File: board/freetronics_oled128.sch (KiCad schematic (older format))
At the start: 38 parts, among them IC1 TPS61040, P1 M02X05, P2 MICROSD, P3 M02X02, P4 M02X02, Q1 2N7002, SW1 SW_PUSHBUTTON, SW2 SW_PUSHBUTTON, U1 MC74VHCT50A

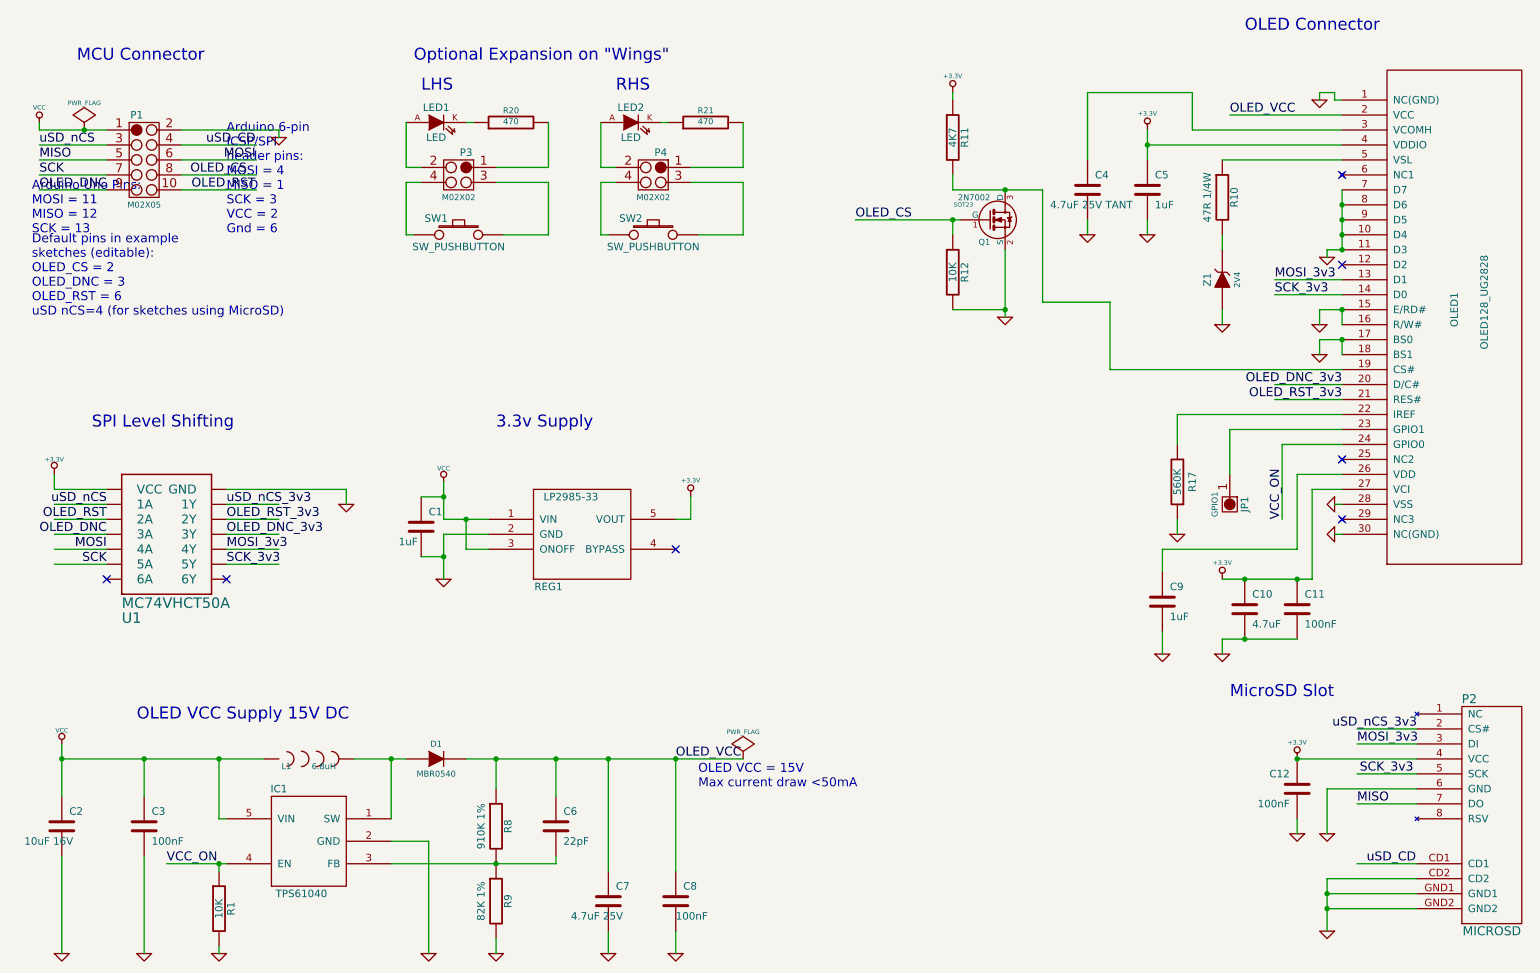
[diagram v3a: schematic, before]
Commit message: Backannotate footprints into schematic, minor labelling cleanups
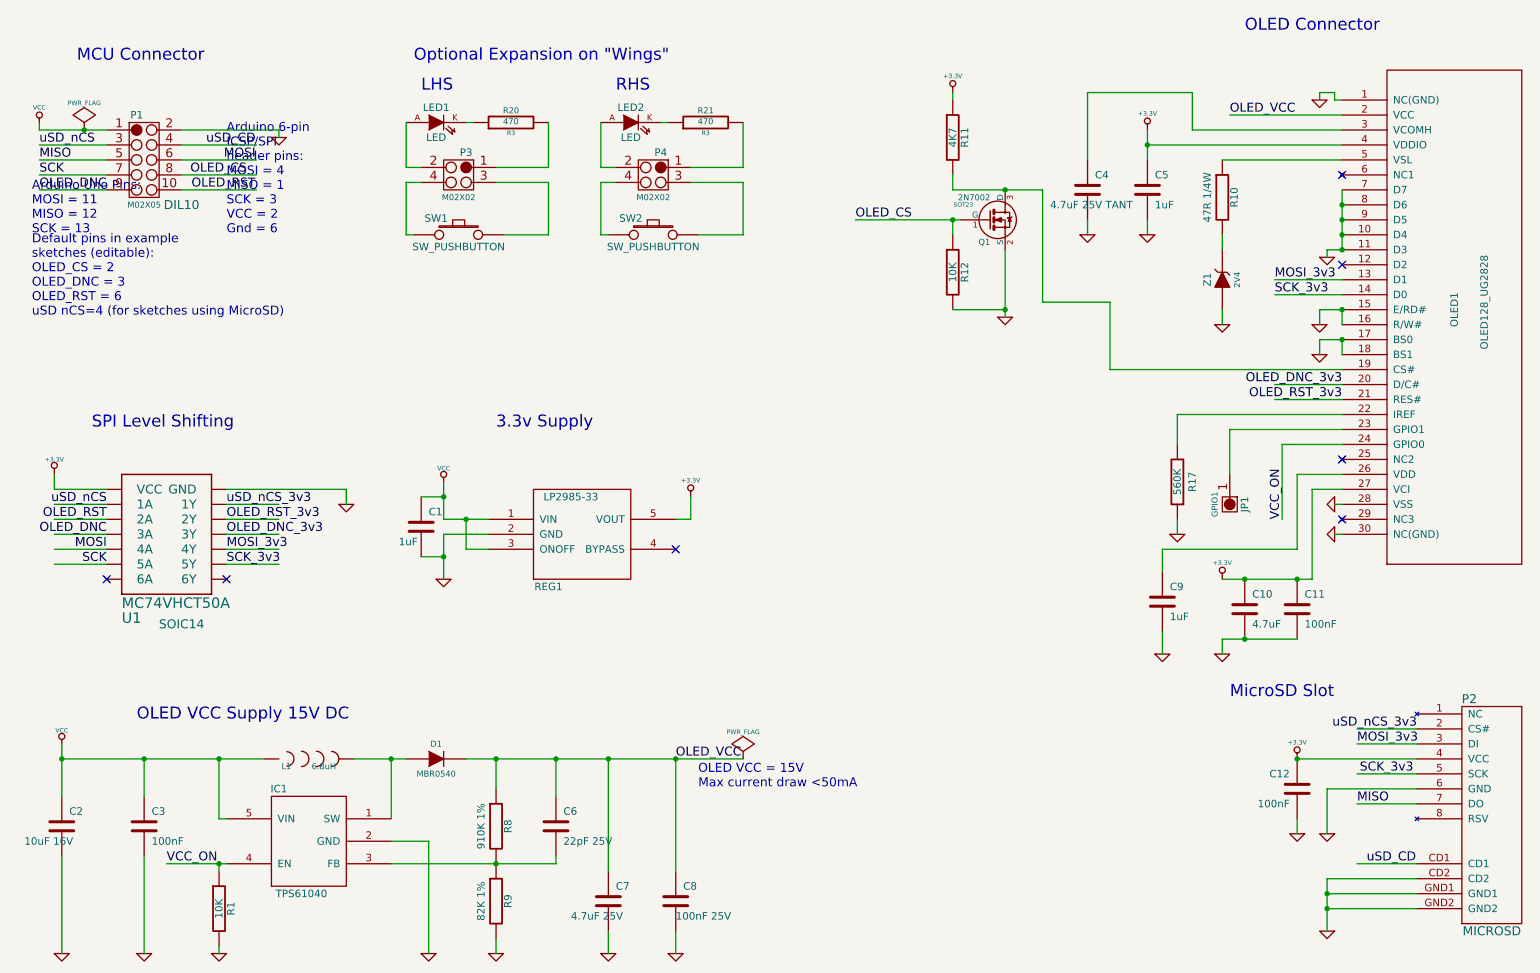
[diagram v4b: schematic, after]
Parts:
- C1, C10, C11, C12, C2, C3, C5, C7, C9, R1, R11, R12, R17, R8, R9: footprint (none) -> 0603
- C4, R10: footprint (none) -> 1206
- C6: value 22pF -> 22pF 25V; footprint (none) -> 0603
- C8: value 100nF -> 100nF 25V; footprint (none) -> 0603
- D1, Z1: footprint (none) -> SOD-123
- IC1: footprint MODULE -> SOT23-5
- JP1: footprint (none) -> 1X01
- L1: footprint (none) -> 1210
- LED1, LED2: footprint (none) -> LED3MM
- OLED1: footprint MODULE -> OLED-128X128-FPC-TOP
- P1: footprint (none) -> DIL10
- P2: footprint (none) -> MICRO-SD-SOCKET-PP
- P3, P4: footprint (none) -> PIN_ARRAY_2X2
- R20, R21: footprint ~ -> R3
- SW1, SW2: footprint (none) -> SW_TC0122
- U1: footprint ~ -> SOIC14
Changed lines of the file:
@@
-EESchema Schematic File Version 2  date Thu 09 May 2013 17:07:11 EST
+EESchema Schematic File Version 2  date Tue 14 May 2013 16:39:14 EST
 LIBS:freetronics_kicad_sch_lib
 LIBS:power
@@
 Sheet 1 1
 Title "Freetronics OLED128              http://www.freetronics.com/oled128"
-Date "9 may 2013"
+Date "14 may 2013"
 Rev "1.2"
 Comp "(C)2013 Freetronics Pty Ltd"
@@
 F 0 "P4" H 4950 1700 50  0000 C CNN
 F 1 "M02X02" H 5000 1400 40  0000 C CNN
-F 2 "" H 5050 1600 60  0001 C CNN
+F 2 "PIN_ARRAY_2X2" H 5050 1600 60  0001 C CNN
 F 3 "" H 5050 1600 60  0001 C CNN
 	1    5050 1600
@@
 F 0 "P3" H 3650 1700 50  0000 C CNN
 F 1 "M02X02" H 3700 1400 40  0000 C CNN
-F 2 "" H 3750 1600 60  0001 C CNN
+F 2 "PIN_ARRAY_2X2" H 3750 1600 60  0001 C CNN
 F 3 "" H 3750 1600 60  0001 C CNN
 	1    3750 1600
@@
 F 0 "LED2" H 4950 1400 50  0000 C CNN
 F 1 "LED" H 4950 1200 50  0000 C CNN
-F 2 "" H 4950 1300 60  0001 C CNN
+F 2 "LED3MM" H 4950 1300 60  0001 C CNN
 F 3 "" H 4950 1300 60  0001 C CNN
 	1    4950 1300
@@
 F 0 "SW2" H 4950 2160 50  0000 C CNN
 F 1 "SW_PUSHBUTTON" H 5100 1970 50  0000 C CNN
-F 2 "" H 5100 2050 60  0001 C CNN
+F 2 "SW_TC0122" H 5100 2050 60  0001 C CNN
 F 3 "" H 5100 2050 60  0001 C CNN
 	1    5100 2050
@@
 F 0 "R21" V 5530 1300 40  0000 C CNN
 F 1 "470" V 5457 1301 40  0000 C CNN
-F 2 "~" V 5380 1300 30  0000 C CNN
+F 2 "R3" V 5380 1300 30  0000 C CNN
 F 3 "~" H 5450 1300 30  0000 C CNN
 	1    5450 1300
@@
 F 0 "R20" V 4230 1300 40  0000 C CNN
 F 1 "470" V 4157 1301 40  0000 C CNN
-F 2 "~" V 4080 1300 30  0000 C CNN
+F 2 "R3" V 4080 1300 30  0000 C CNN
 F 3 "~" H 4150 1300 30  0000 C CNN
 	1    4150 1300
@@
 F 0 "SW1" H 3650 2160 50  0000 C CNN
 F 1 "SW_PUSHBUTTON" H 3800 1970 50  0000 C CNN
-F 2 "" H 3800 2050 60  0001 C CNN
+F 2 "SW_TC0122" H 3800 2050 60  0001 C CNN
 F 3 "" H 3800 2050 60  0001 C CNN
 	1    3800 2050
@@
 F 0 "LED1" H 3650 1400 50  0000 C CNN
 F 1 "LED" H 3650 1200 50  0000 C CNN
-F 2 "" H 3650 1300 60  0001 C CNN
+F 2 "LED3MM" H 3650 1300 60  0001 C CNN
 F 3 "" H 3650 1300 60  0001 C CNN
 	1    3650 1300
@@
 F 0 "D1" H 3650 5650 40  0000 C CNN
 F 1 "MBR0540" H 3650 5450 40  0000 C CNN
-F 2 "" H 3650 5550 60  0001 C CNN
+F 2 "SOD-123" H 3650 5550 60  0001 C CNN
 F 3 "" H 3650 5550 60  0001 C CNN
 	1    3650 5550
@@
 F 0 "P2" H 10750 6950 60  0000 C CNN
 F 1 "MICROSD" H 10600 5400 60  0000 C CNN
-F 2 "" H 10650 6050 60  0001 C CNN
+F 2 "MICRO-SD-SOCKET-PP" H 10650 6050 60  0001 C CNN
 F 3 "" H 10650 6050 60  0001 C CNN
 	1    10650 6050
@@
 F 0 "JP1" H 8850 4050 50  0000 C CNN
 F 1 "GPIO1" H 8850 3850 40  0000 C CNN
-F 2 "" H 8950 3950 60  0001 C CNN
+F 2 "1X01" H 8950 3950 60  0001 C CNN
 F 3 "" H 8950 3950 60  0001 C CNN
 	1    8950 3950
@@
 F 0 "C12" H 9450 5850 50  0000 L CNN
 F 1 "100nF" H 9450 5650 50  0000 L CNN
-F 2 "" H 9400 5750 60  0001 C CNN
+F 2 "0603" H 9400 5750 60  0001 C CNN
 F 3 "" H 9400 5750 60  0001 C CNN
 	1    9400 5750
@@
 F 0 "R12" V 7180 2300 50  0000 C CNN
 F 1 "10K" V 7100 2300 50  0000 C CNN
-F 2 "" H 7100 2300 60  0001 C CNN
+F 2 "0603" H 7100 2300 60  0001 C CNN
 F 3 "" H 7100 2300 60  0001 C CNN
 	1    7100 2300
@@
 F 0 "R11" V 7180 1400 50  0000 C CNN
 F 1 "4K7" V 7100 1400 50  0000 C CNN
-F 2 "" H 7100 1400 60  0001 C CNN
+F 2 "0603" H 7100 1400 60  0001 C CNN
 F 3 "" H 7100 1400 60  0001 C CNN
 	1    7100 1400
@@
 F 0 "C1" H 3600 4100 50  0000 L CNN
 F 1 "1uF" H 3400 3900 50  0000 L CNN
-F 2 "" H 3550 4000 60  0001 C CNN
+F 2 "0603" H 3550 4000 60  0001 C CNN
 F 3 "" H 3550 4000 60  0001 C CNN
 	1    3550 4000
@@
 F 0 "R1" V 2280 6550 50  0000 C CNN
 F 1 "10K" V 2200 6550 50  0000 C CNN
-F 2 "" H 2200 6550 60  0001 C CNN
+F 2 "0603" H 2200 6550 60  0001 C CNN
 F 3 "" H 2200 6550 60  0001 C CNN
 	1    2200 6550
@@
 P 5250 6500
 F 0 "C8" H 5300 6600 50  0000 L CNN
-F 1 "100nF" H 5250 6400 50  0000 L CNN
-F 2 "" H 5250 6500 60  0001 C CNN
+F 1 "100nF 25V" H 5250 6400 50  0000 L CNN
+F 2 "0603" H 5250 6500 60  0001 C CNN
 F 3 "" H 5250 6500 60  0001 C CNN
 	1    5250 6500
@@
 F 0 "C7" H 4850 6600 50  0000 L CNN
 F 1 "4.7uF  25V" H 4550 6400 50  0000 L CNN
-F 2 "" H 4800 6500 60  0001 C CNN
+F 2 "0603" H 4800 6500 60  0001 C CNN
 F 3 "" H 4800 6500 60  0001 C CNN
 	1    4800 6500
@@
 P 4450 6000
 F 0 "C6" H 4500 6100 50  0000 L CNN
-F 1 "22pF" H 4500 5900 50  0000 L CNN
-F 2 "" H 4450 6000 60  0001 C CNN
+F 1 "22pF 25V" H 4500 5900 50  0000 L CNN
+F 2 "0603" H 4450 6000 60  0001 C CNN
 F 3 "" H 4450 6000 60  0001 C CNN
 	1    4450 6000
@@
 F 0 "R9" V 4130 6500 50  0000 C CNN
 F 1 "82K 1%" V 3950 6500 50  0000 C CNN
-F 2 "" H 4050 6500 60  0001 C CNN
+F 2 "0603" H 4050 6500 60  0001 C CNN
 F 3 "" H 4050 6500 60  0001 C CNN
 	1    4050 6500
@@
 F 0 "R8" V 4130 6000 50  0000 C CNN
 F 1 "910K 1%" V 3950 6000 50  0000 C CNN
-F 2 "" H 4050 6000 60  0001 C CNN
+F 2 "0603" H 4050 6000 60  0001 C CNN
 F 3 "" H 4050 6000 60  0001 C CNN
 	1    4050 6000
@@
 F 0 "C3" H 1750 6100 50  0000 L CNN
 F 1 "100nF" H 1750 5900 50  0000 L CNN
-F 2 "" H 1700 6000 60  0001 C CNN
+F 2 "0603" H 1700 6000 60  0001 C CNN
 F 3 "" H 1700 6000 60  0001 C CNN
 	1    1700 6000
@@
 F 0 "C2" H 1200 6100 50  0000 L CNN
 F 1 "10uF  16V" H 900 5900 50  0000 L CNN
-F 2 "" H 1150 6000 60  0001 C CNN
+F 2 "0603" H 1150 6000 60  0001 C CNN
 F 3 "" H 1150 6000 60  0001 C CNN
 	1    1150 6000
@@
 F 0 "IC1" H 2600 6450 50  0000 C CNN
 F 1 "TPS61040" H 2750 5750 50  0000 C CNN
-F 2 "MODULE" H 2800 5850 50  0001 C CNN
+F 2 "SOT23-5" H 2800 5850 50  0001 C CNN
 F 3 "DOCUMENTATION" H 2800 6350 50  0001 C CNN
 	1    3000 6100
@@
 F 0 "L1" H 2650 5500 40  0000 C CNN
 F 1 "6.8uH" H 2900 5500 40  0000 C CNN
-F 2 "" H 2800 5550 60  0001 C CNN
+F 2 "1210" H 2800 5550 60  0001 C CNN
 F 3 "6.8uH 1210 NLCV32T-6R8M-PF" H 2800 5550 60  0001 C CNN
 	1    2800 5550
@@
 F 0 "C11" H 9450 4650 50  0000 L CNN
 F 1 "100nF" H 9450 4450 50  0000 L CNN
-F 2 "" H 9400 4550 60  0001 C CNN
+F 2 "0603" H 9400 4550 60  0001 C CNN
 F 3 "" H 9400 4550 60  0001 C CNN
 	1    9400 4550
@@
 F 0 "C10" H 9100 4650 50  0000 L CNN
 F 1 "4.7uF" H 9100 4450 50  0000 L CNN
-F 2 "" H 9050 4550 60  0001 C CNN
+F 2 "0603" H 9050 4550 60  0001 C CNN
 F 3 "" H 9050 4550 60  0001 C CNN
 	1    9050 4550
@@
 F 0 "C9" H 8550 4600 50  0000 L CNN
 F 1 "1uF" H 8550 4400 50  0000 L CNN
-F 2 "" H 8500 4500 60  0001 C CNN
+F 2 "0603" H 8500 4500 60  0001 C CNN
 F 3 "" H 8500 4500 60  0001 C CNN
 	1    8500 4500
@@
 F 0 "R17" V 8500 3700 50  0000 C CNN
 F 1 "560K" V 8600 3700 50  0000 C CNN
-F 2 "" H 8600 3700 60  0001 C CNN
+F 2 "0603" H 8600 3700 60  0001 C CNN
 F 3 "" H 8600 3700 60  0001 C CNN
 	1    8600 3700
@@
 F 0 "Z1" H 8900 2450 50  0000 C CNN
 F 1 "2V4" H 8900 2250 40  0000 C CNN
-F 2 "" H 8900 2350 60  0001 C CNN
+F 2 "SOD-123" H 8900 2350 60  0001 C CNN
 F 3 "" H 8900 2350 60  0001 C CNN
 	1    8900 2350
@@
 F 0 "R10" V 8980 1800 50  0000 C CNN
 F 1 "47R  1/4W" V 8800 1800 50  0000 C CNN
-F 2 "" H 8900 1800 60  0001 C CNN
+F 2 "1206" H 8900 1800 60  0001 C CNN
 F 3 "" H 8900 1800 60  0001 C CNN
 	1    8900 1800
@@
 F 0 "C5" H 8450 1850 50  0000 L CNN
 F 1 "1uF" H 8450 1650 50  0000 L CNN
-F 2 "" H 8400 1750 60  0001 C CNN
+F 2 "0603" H 8400 1750 60  0001 C CNN
 F 3 "" H 8400 1750 60  0001 C CNN
 	1    8400 1750
@@
 F 0 "C4" H 8050 1850 50  0000 L CNN
 F 1 "4.7uF 25V TANT" H 7750 1650 50  0000 L CNN
-F 2 "" H 8000 1750 60  0001 C CNN
+F 2 "1206" H 8000 1750 60  0001 C CNN
 F 3 "" H 8000 1750 60  0001 C CNN
 	1    8000 1750
@@
 F 0 "OLED1" V 10450 2650 50  0000 C CNN
 F 1 "OLED128_UG2828" V 10650 2700 50  0000 C CNN
-F 2 "MODULE" H 10450 2600 50  0001 C CNN
+F 2 "OLED-128X128-FPC-TOP" H 10450 2600 50  0001 C CNN
 F 3 "DOCUMENTATION" H 10450 2600 50  0001 C CNN
 F 4 "SSD1351" H 10450 2600 50  0001 C CNN "Controller"
@@
 F 0 "P1" H 1650 1450 50  0000 C CNN
 F 1 "M02X05" H 1700 850 40  0000 C CNN
-F 2 "" H 1750 1350 60  0000 C CNN
+F 2 "DIL10" H 1950 850 60  0000 C CNN
 F 3 "" H 1750 1350 60  0000 C CNN
 	1    1750 1350
@@
 F 0 "U1" H 1550 3450 70  0000 L BNN
 F 1 "MC74VHCT50A" H 1550 3550 70  0000 L BNN
-F 2 "~" H 1850 4050 60  0000 C CNN
+F 2 "SOIC14" H 1950 3450 60  0000 C CNN
 F 3 "~" H 1850 4050 60  0000 C CNN
 	1    1850 4050

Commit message: Clean up nomenclature
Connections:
- net labels added: OLED_DnC, OLED_DnC_3v3, OLED_nRST, OLED_nRST_3v3
- net labels removed: OLED_DNC, OLED_DNC_3v3, OLED_RST, OLED_RST_3v3
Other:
- note added: "Default pins in example\nsketches (editable):\nOLED_CS = 2\nOLED_DnC = 3\nOLED_nRST = 6\nuSD nCS=4 (for sketches using MicroSD)"
- note removed: "Default pins in example\nsketches (editable):\nOLED_CS = 2\nOLED_DNC = 3\nOLED_RST = 6\nuSD nCS=4 (for sketches using MicroSD)"
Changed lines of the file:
@@
-EESchema Schematic File Version 2  date Tue 14 May 2013 16:39:14 EST
+EESchema Schematic File Version 2  date Mon 20 May 2013 08:44:48 EST
 LIBS:freetronics_kicad_sch_lib
 LIBS:power
@@
 Sheet 1 1
 Title "Freetronics OLED128              http://www.freetronics.com/oled128"
-Date "14 may 2013"
+Date "19 may 2013"
 Rev "1.2"
 Comp "(C)2013 Freetronics Pty Ltd"
@@
 NoConn ~ 9700 3550
 Text Label 2016 1750 0    60   ~ 0
-OLED_RST
+OLED_nRST
 Text Label 1000 1750 0    60   ~ 0
-OLED_DNC
+OLED_DnC
 Text Label 2008 1650 0    60   ~ 0
 OLED_CS
@@
 $EndComp
 Text Label 1450 3950 2    60   ~ 0
-OLED_RST
+OLED_nRST
 Text Label 1450 4050 2    60   ~ 0
-OLED_DNC
+OLED_DnC
 Text Label 1450 4250 2    60   ~ 0
 SCK
@@
 	9700 3050 9250 3050
 Text Label 9700 3050 2    60   ~ 0
-OLED_DNC_3v3
+OLED_DnC_3v3
 Text Label 9700 3150 2    60   ~ 0
-OLED_RST_3v3
+OLED_nRST_3v3
 Text Label 2250 4050 0    60   ~ 0
-OLED_DNC_3v3
+OLED_DnC_3v3
 Text Label 2250 3950 0    60   ~ 0
-OLED_RST_3v3
+OLED_nRST_3v3
 $Comp
 L VCC #PWR035
@@
 Arduino 6-pin\nICSP/SPI\nheader pins:\nMOSI = 4\nMISO = 1\nSCK = 3\nVCC = 2\nGnd = 6
 Text Notes 950  2600 0    60   ~ 0
-Default pins in example\nsketches (editable):\nOLED_CS = 2\nOLED_DNC = 3\nOLED_RST = 6\nuSD nCS=4 (for sketches using MicroSD)
+Default pins in example\nsketches (editable):\nOLED_CS = 2\nOLED_DnC = 3\nOLED_nRST = 6\nuSD nCS=4 (for sketches using MicroSD)
 $EndSCHEMATC
